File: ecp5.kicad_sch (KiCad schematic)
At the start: 32 parts, among them U201 LFE5U-25F-6BGA256C

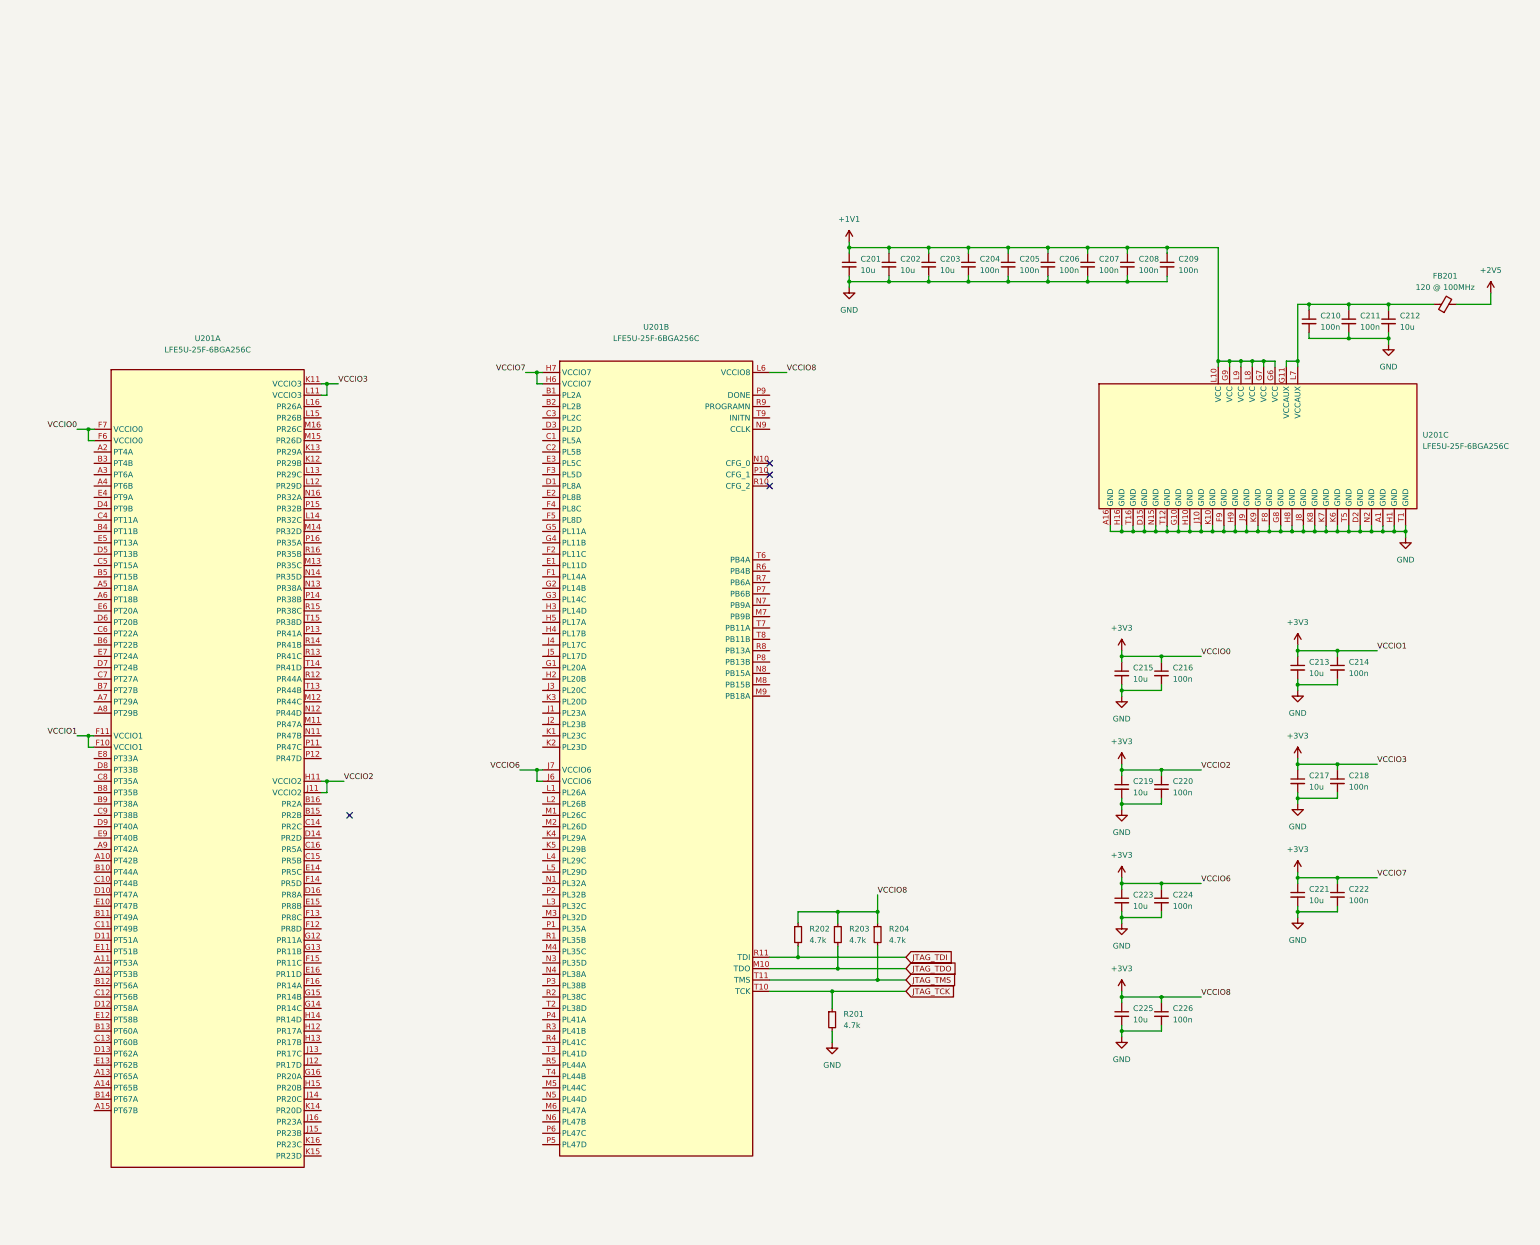
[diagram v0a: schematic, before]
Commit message: Towards routing RAM
 - Moved the RAM to its own sheet
 - Use the ECP5 prefix to capture impedance controlled traces
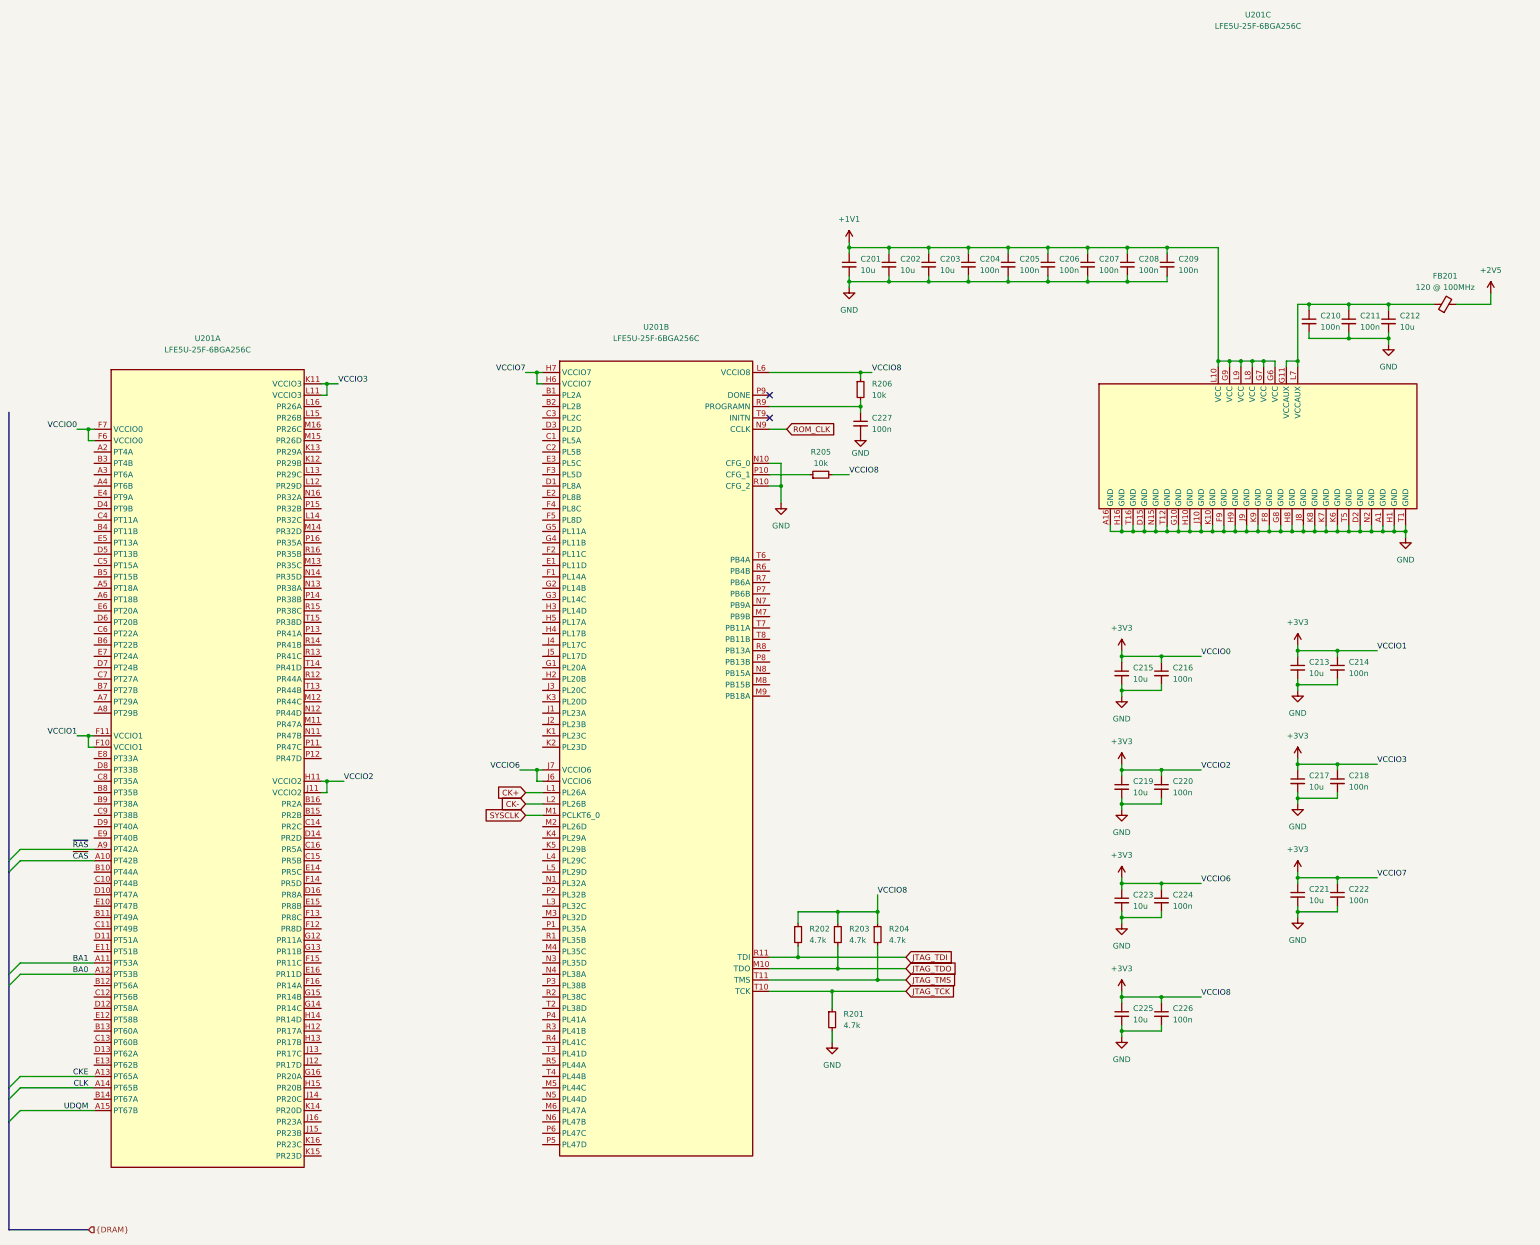
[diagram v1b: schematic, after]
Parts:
- added C227: 100n, Capacitor_SMD:C_0201_0603Metric, symbol Device:C_Small
- added R205, R206: 10k, Resistor_SMD:R_0201_0603Metric, symbol Device:R_Small
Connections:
- net +3V3: now also R205.2, R206.1
- net GND: now also U201.N10 (CFG_0), U201.R10 (CFG_2), C227.2
- net ~{CAS}: now reaches U201.A10 (PT42B)
- net BA1: now reaches U201.A11 (PT53A)
- net BA0: now reaches U201.A12 (PT53B)
- net CKE: now reaches U201.A13 (PT65A)
- net CLK: now reaches U201.A14 (PT65B)
- net UDQM: now reaches U201.A15 (PT67B)
- net ~{RAS}: now reaches U201.A9 (PT42A)
- net CK+: now reaches U201.L1 (PL26A)
- net CK-: now reaches U201.L2 (PL26B)
- net SYSCLK: now reaches U201.M1 (PL26C)
- net ROM_CLK: now reaches U201.N9 (CCLK)
- net at U201.P10 (CFG_1): now also R205.1
- net at U201.R9 (PROGRAMN): now also C227.1, R206.2
- no-connect marks 4 -> 2

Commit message: First whole routing
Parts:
- removed C207, C208, C209, C220: 100n, Capacitor_SMD:C_0201_0603Metric, symbol Device:C_Small
- removed C215, C221, C225: 10u, Capacitor_SMD:C_0603_1608Metric, symbol Device:C_Small
- removed R201, R202, R203, R204: 4.7k, Resistor_SMD:R_0402_1005Metric, symbol Device:R_Small
- C201, C202, C203, C212, C213, C217, C219, C223: footprint Capacitor_SMD:C_0603_1608Metric -> Capacitor_SMD:C_0402_1005Metric
- U201: MFN C1521614 -> (none); MPN (none) -> C1521614
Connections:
- net +3V3: no longer C213.1, C214.1, U201.F10 (VCCIO1), U201.F11 (VCCIO1)
- net PROGRAMN: now reaches C227.1, R206.2, U201.R9 (PROGRAMN)
- net HDMI_D2+: now reaches U201.A2 (PT4A)
- net HDMI_D1+: now reaches U201.A3 (PT6A)
- net HDMI_D1-: now reaches U201.A4 (PT6B)
- net HDMI_D0+: now reaches U201.A5 (PT18A)
- net HDMI_D0-: now reaches U201.A6 (PT18B)
- net HDMI_CK+: now reaches U201.A7 (PT29A)
- net HDMI_CK-: now reaches U201.A8 (PT29B)
- net DQ1: now reaches U201.B11 (PT49A)
- net DQ6: now reaches U201.B13 (PT60A)
- net DQ4: now reaches U201.B14 (PT67A)
- net GPIO8: now reaches U201.B15 (PR2B)
- net GPIO9: now reaches U201.B16 (PR2A)
- net HDMI_D2-: now reaches U201.B3 (PT4B)
- net CK_P: now reaches U201.B8 (PT35B)
- net DQ5: now reaches U201.C13 (PT60B)
- net GPIO7: now reaches U201.C14 (PR2C)
- net GPIO0: now reaches U201.C15 (PR5B)
- net GPIO15: now reaches U201.C16 (PR5A)
- net CK_N: now reaches U201.C8 (PT35A)
- net CS#: now reaches U201.D13 (PT62A)
- net GPIO16: now reaches U201.D14 (PR2D)
- net GPIO1: now reaches U201.D16 (PR8A)
- net RESET#: now reaches U201.E13 (PT62B)
- net GPIO2: now reaches U201.E15 (PR8B)
- net GPIO3: now reaches U201.E16 (PR11D)
- net GPIO4: now reaches U201.F15 (PR11C)
- net GPIO5: now reaches U201.F16 (PR14A)
- net GPIO12: now reaches U201.G16 (PR20A)
- net GPIO13: now reaches U201.M16 (PR26C)
- net SDA0: now reaches U201.N13 (PR38A)
- net GPIO6: now reaches U201.N14 (PR35D)
- net GPIO14: now reaches U201.N16 (PR32A)
- net SCL0: now reaches U201.P14 (PR38B)
- net GPIO11: now reaches U201.P15 (PR32B)
- net GPIO10: now reaches U201.P16 (PR35A)
- net GPIO25: now reaches U201.R13 (PR41C)
- net GPIO23: now reaches U201.R14 (PR41B)
- net GPIO26: now reaches U201.R15 (PR38C)
- net GPIO21: now reaches U201.R16 (PR35B)
- net GPIO29: now reaches U201.T13 (PR44B)
- net GPIO28: now reaches U201.T14 (PR41D)
- net GPIO22: now reaches U201.T15 (PR38D)
- net SD_DAT2: now reaches U201.B1 (PL2A)
- net SD_CS: now reaches U201.B2 (PL2B)
- net SD_DET: now reaches U201.C1 (PL5A)
- net SD_MOSI: now reaches U201.C2 (PL5B)
- net SD_CLK: now reaches U201.C3 (PL2C)
- net USER_LED2: now reaches U201.D1 (PL8A)
- net SD_MISO: now reaches U201.D3 (PL2D)
- net USER_LED1: now reaches U201.E1 (PL11D)
- net SD_DAT1: now reaches U201.E3 (PL5C)
- net CFG_1: now reaches R205.1, U201.P10 (CFG_1)
- net USB1_DP: now reaches U201.R5 (PL44A)
- net ROM_MOSI: now reaches U201.R8 (PB13A)
- net UART_RX: now reaches U201.T2 (PL38D)
- net USB1_SEL: now reaches U201.T3 (PL41D)
- net USB1_DN: now reaches U201.T4 (PL44B)
- net ROM_CS#: now reaches U201.T7 (PB11A)
- net ROM_MISO: now reaches U201.T8 (PB11B)
- net VCCAUX: now reaches C210.1, C211.1, C212.1, FB201.1, U201.G11 (VCCAUX), U201.L7 (VCCAUX)
- net BA0 renamed DQ0
- net BA1 renamed DQ7
- net CKE renamed RWDS
- net CLK renamed DQ3
- net UDQM renamed DQ2
- net ~{CAS}: no longer names the net of U201.A10 (PT42B)
- net ~{RAS}: no longer names the net of U201.A9 (PT42A)
- new net +1V8: C213.1, C214.1, U201.F10 (VCCIO1), U201.F11 (VCCIO1)
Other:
- note added: "This will hold PROGRAMN down until VCCIO8 is high enough, waiving the need for proper sequencing."
- moved on the sheet: C201, C202, C203, C204, C205, C206, C219, C222, C226

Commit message: Update some component values and complete MPN for BOM
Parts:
- C201, C202, C203, C212, C213, C217, C219, C223: value 10u -> 10uF; MPN (none) -> C15525
- C204, C205, C206, C210, C211, C214, C216, C218, C222, C224, C226, C227: value 100n -> 100nF; MPN (none) -> C190183
- FB201: value 120 @ 100MHz -> 100 @ 100MHz; footprint Inductor_SMD:L_0402_1005Metric -> Inductor_SMD:L_0805_2012Metric; MPN (none) -> C1015
- R205, R206: MPN (none) -> C473048

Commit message: Minor fixes
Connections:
- net UART_RX renamed UART_TX
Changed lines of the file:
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@@
 	(generator_version "8.0")
 	(paper "A3")
+	(bus_alias "JTAG"
+		(members "TDI" "TDO" "TMS" "TCK")
+	)
 	(junction
 		(at 311.15 132.08)
@@
 		)
 	)
-	(global_label "UART_RX"
+	(global_label "UART_TX"
 		(shape input)
 		(at 177.8 203.2 180)
@@
 		)
 		(property "Intersheetrefs" "${INTERSHEET_REFS}"
-			(at 166.711 203.2 0)
+			(at 167.0134 203.2 0)
 			(effects
 				(font
